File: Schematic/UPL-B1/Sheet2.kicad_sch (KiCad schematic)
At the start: 40 parts, among them K2 G5V-2_Split, P20 TestPoint, P21 TestPoint, X2 Conn_01x03_Pin_Bridge

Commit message: added majority of footprints
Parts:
- C200, C201, C202, C203, C204, C205: footprint (none) -> Capacitor_THT:C_Radial_D6.3mm_H11.0mm_P2.50mm
- C206, C207, C208, C209, C210, C211, C212, C215, C216: footprint (none) -> Capacitor_SMD:C_1206_3216Metric_Pad1.33x1.80mm_HandSolder
- D20: footprint (none) -> Package_SO:SOIC-14_3.9x8.7mm_P1.27mm
- D22: footprint SOIC127P1032X265-16N -> Package_SO:SOIC-16W_7.5x10.3mm_P1.27mm
- D23: footprint (none) -> Package_SO:SOIC-16_3.9x9.9mm_P1.27mm
- N20: footprint (none) -> Package_SO:SOIC-8_3.9x4.9mm_P1.27mm
- P20, P21: footprint (none) -> Connector_PinHeader_1.00mm:PinHeader_1x01_P1.00mm_Vertical
- R200, R201, R202, R203, R204, R205, R206, R207, R208, R209, R210, R211, R212, R215: footprint (none) -> Resistor_SMD:R_1206_3216Metric_Pad1.30x1.75mm_HandSolder
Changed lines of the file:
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@@
 			)
 		)
-		(property "Footprint" ""
+		(property "Footprint" "Package_SO:SOIC-14_3.9x8.7mm_P1.27mm"
 			(at 63.5 177.8 0)
 			(effects
@@
 			)
 		)
-		(property "Footprint" ""
+		(property "Footprint" "Resistor_SMD:R_1206_3216Metric_Pad1.30x1.75mm_HandSolder"
 			(at 328.93 227.838 90)
 			(effects
@@
 			)
 		)
-		(property "Footprint" ""
+		(property "Footprint" "Capacitor_SMD:C_1206_3216Metric_Pad1.33x1.80mm_HandSolder"
 			(at 360.68 179.07 0)
 			(effects
@@
 			)
 		)
-		(property "Footprint" ""
+		(property "Footprint" "Capacitor_SMD:C_1206_3216Metric_Pad1.33x1.80mm_HandSolder"
 			(at 116.84 35.56 0)
 			(effects
@@
 			)
 		)
-		(property "Footprint" ""
+		(property "Footprint" "Capacitor_SMD:C_1206_3216Metric_Pad1.33x1.80mm_HandSolder"
 			(at 351.79 106.68 0)
 			(effects
@@
 			)
 		)
-		(property "Footprint" ""
+		(property "Footprint" "Package_SO:SOIC-14_3.9x8.7mm_P1.27mm"
 			(at 41.91 208.28 0)
 			(effects
@@
 			)
 		)
-		(property "Footprint" ""
+		(property "Footprint" "Resistor_SMD:R_1206_3216Metric_Pad1.30x1.75mm_HandSolder"
 			(at 328.93 215.138 90)
 			(effects
@@
 			)
 		)
-		(property "Footprint" ""
+		(property "Footprint" "Capacitor_THT:C_Radial_D6.3mm_H11.0mm_P2.50mm"
 			(at 29.21 33.02 0)
 			(effects
@@
 			)
 		)
-		(property "Footprint" ""
+		(property "Footprint" "Resistor_SMD:R_1206_3216Metric_Pad1.30x1.75mm_HandSolder"
 			(at 232.918 114.3 90)
 			(effects
@@
 			)
 		)
-		(property "Footprint" ""
+		(property "Footprint" "Package_SO:SOIC-8_3.9x4.9mm_P1.27mm"
 			(at 347.98 120.65 0)
 			(effects
@@
 			)
 		)
-		(property "Footprint" ""
+		(property "Footprint" "Resistor_SMD:R_1206_3216Metric_Pad1.30x1.75mm_HandSolder"
 			(at 96.52 27.94 0)
 			(effects
@@
 			)
 		)
-		(property "Footprint" ""
+		(property "Footprint" "Resistor_SMD:R_1206_3216Metric_Pad1.30x1.75mm_HandSolder"
 			(at 236.728 165.1 90)
 			(effects
@@
 			)
 		)
-		(property "Footprint" ""
+		(property "Footprint" "Connector_PinHeader_1.00mm:PinHeader_1x01_P1.00mm_Vertical"
 			(at 121.92 22.86 0)
 			(effects
@@
 			)
 		)
-		(property "Footprint" ""
+		(property "Footprint" "Resistor_SMD:R_1206_3216Metric_Pad1.30x1.75mm_HandSolder"
 			(at 231.14 74.168 90)
 			(effects
@@
 			)
 		)
-		(property "Footprint" ""
+		(property "Footprint" "Resistor_SMD:R_1206_3216Metric_Pad1.30x1.75mm_HandSolder"
 			(at 148.59 129.54 0)
 			(effects
@@
 			)
 		)
-		(property "Footprint" ""
+		(property "Footprint" "Package_SO:SOIC-16_3.9x9.9mm_P1.27mm"
 			(at 354.33 208.28 0)
 			(effects
@@
 			)
 		)
-		(property "Footprint" ""
+		(property "Footprint" "Resistor_SMD:R_1206_3216Metric_Pad1.30x1.75mm_HandSolder"
 			(at 38.1 69.85 0)
 			(effects
@@
 			)
 		)
-		(property "Footprint" ""
+		(property "Footprint" "Capacitor_SMD:C_1206_3216Metric_Pad1.33x1.80mm_HandSolder"
 			(at 152.4 38.1 0)
 			(effects
@@
 			)
 		)
-		(property "Footprint" ""
+		(property "Footprint" "Capacitor_THT:C_Radial_D6.3mm_H11.0mm_P2.50mm"
 			(at 45.72 33.02 0)
 			(effects
@@
 			)
 		)
-		(property "Footprint" ""
+		(property "Footprint" "Resistor_SMD:R_1206_3216Metric_Pad1.30x1.75mm_HandSolder"
 			(at 85.09 69.85 0)
 			(effects
@@
 			)
 		)
-		(property "Footprint" ""
+		(property "Footprint" "Resistor_SMD:R_1206_3216Metric_Pad1.30x1.75mm_HandSolder"
 			(at 128.27 69.85 0)
 			(effects
@@
 			)
 		)
-		(property "Footprint" ""
+		(property "Footprint" "Connector_PinHeader_1.00mm:PinHeader_1x01_P1.00mm_Vertical"
 			(at 394.97 66.04 0)
 			(effects
@@
 			)
 		)
-		(property "Footprint" ""
+		(property "Footprint" "Capacitor_SMD:C_1206_3216Metric_Pad1.33x1.80mm_HandSolder"
 			(at 151.13 77.47 0)
 			(effects
@@
 			)
 		)
-		(property "Footprint" ""
+		(property "Footprint" "Package_SO:SOIC-14_3.9x8.7mm_P1.27mm"
 			(at 168.91 38.1 0)
 			(effects
@@
 			)
 		)
-		(property "Footprint" ""
+		(property "Footprint" "Package_SO:SOIC-14_3.9x8.7mm_P1.27mm"
 			(at 41.91 226.06 0)
 			(effects
@@
 			)
 		)
-		(property "Footprint" ""
+		(property "Footprint" "Capacitor_THT:C_Radial_D6.3mm_H11.0mm_P2.50mm"
 			(at 92.71 77.47 0)
 			(effects
@@
 			)
 		)
-		(property "Footprint" ""
+		(property "Footprint" "Capacitor_THT:C_Radial_D6.3mm_H11.0mm_P2.50mm"
 			(at 60.96 33.02 0)
 			(effects
@@
 			)
 		)
-		(property "Footprint" ""
+		(property "Footprint" "Resistor_SMD:R_1206_3216Metric_Pad1.30x1.75mm_HandSolder"
 			(at 41.91 175.26 0)
 			(effects
@@
 			)
 		)
-		(property "Footprint" ""
+		(property "Footprint" "Resistor_SMD:R_1206_3216Metric_Pad1.30x1.75mm_HandSolder"
 			(at 104.14 35.56 0)
 			(effects
@@
 			)
 		)
-		(property "Footprint" "SOIC127P1032X265-16N"
+		(property "Footprint" "Package_SO:SOIC-16W_7.5x10.3mm_P1.27mm"
 			(at 279.4 129.54 0)
 			(effects
@@
 			)
 		)
-		(property "Footprint" ""
+		(property "Footprint" "Capacitor_THT:C_Radial_D6.3mm_H11.0mm_P2.50mm"
 			(at 45.72 77.47 0)
 			(effects
@@
 			)
 		)
-		(property "Footprint" ""
+		(property "Footprint" "Capacitor_SMD:C_1206_3216Metric_Pad1.33x1.80mm_HandSolder"
 			(at 322.58 107.95 0)
 			(effects
@@
 			)
 		)
-		(property "Footprint" ""
+		(property "Footprint" "Capacitor_SMD:C_1206_3216Metric_Pad1.33x1.80mm_HandSolder"
 			(at 356.87 134.62 0)
 			(effects
@@
 			)
 		)
-		(property "Footprint" ""
+		(property "Footprint" "Capacitor_THT:C_Radial_D6.3mm_H11.0mm_P2.50mm"
 			(at 135.89 77.47 0)
 			(effects
@@
 			)
 		)
-		(property "Footprint" ""
+		(property "Footprint" "Capacitor_SMD:C_1206_3216Metric_Pad1.33x1.80mm_HandSolder"
 			(at 110.49 116.84 0)
 			(effects
@@
 			)
 		)
-		(property "Footprint" ""
+		(property "Footprint" "Package_SO:SOIC-14_3.9x8.7mm_P1.27mm"
 			(at 41.91 191.77 0)
 			(effects
@@
 			)
 		)
-		(property "Footprint" ""
+		(property "Footprint" "Resistor_SMD:R_1206_3216Metric_Pad1.30x1.75mm_HandSolder"
 			(at 29.21 234.95 0)
 			(effects
@@
 			)
 		)
-		(property "Footprint" ""
+		(property "Footprint" "Resistor_SMD:R_1206_3216Metric_Pad1.30x1.75mm_HandSolder"
 			(at 328.93 204.978 90)
 			(effects
@@
 			)
 		)
-		(property "Footprint" ""
+		(property "Footprint" "Capacitor_SMD:C_1206_3216Metric_Pad1.33x1.80mm_HandSolder"
 			(at 351.79 146.05 0)
 			(effects

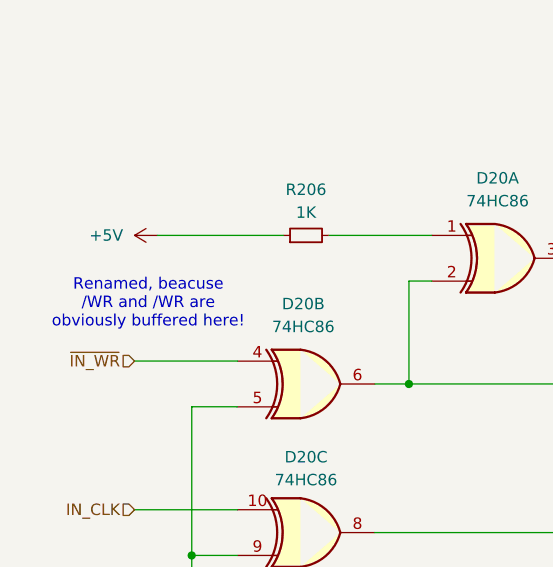
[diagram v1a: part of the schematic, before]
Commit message: Rough component outline on PCB
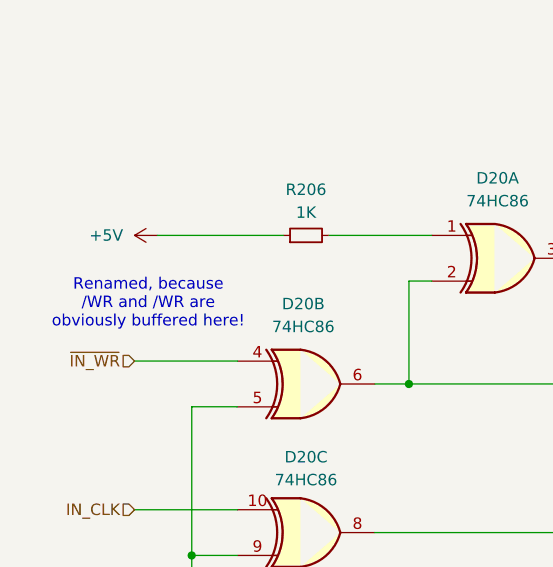
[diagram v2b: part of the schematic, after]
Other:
- note added: "Renamed, because /WR and /WR are obviously buffered here!"
- note removed: "Renamed, beacuse /WR and /WR are obviously buffered here!"
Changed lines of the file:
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@@
 		(company "BVKSound")
 	)
-	(text "Renamed, beacuse \n/WR and /WR are \nobviously buffered here!"
+	(text "Renamed, because \n/WR and /WR are \nobviously buffered here!"
 		(exclude_from_sim no)
 		(at 24.384 182.88 0)

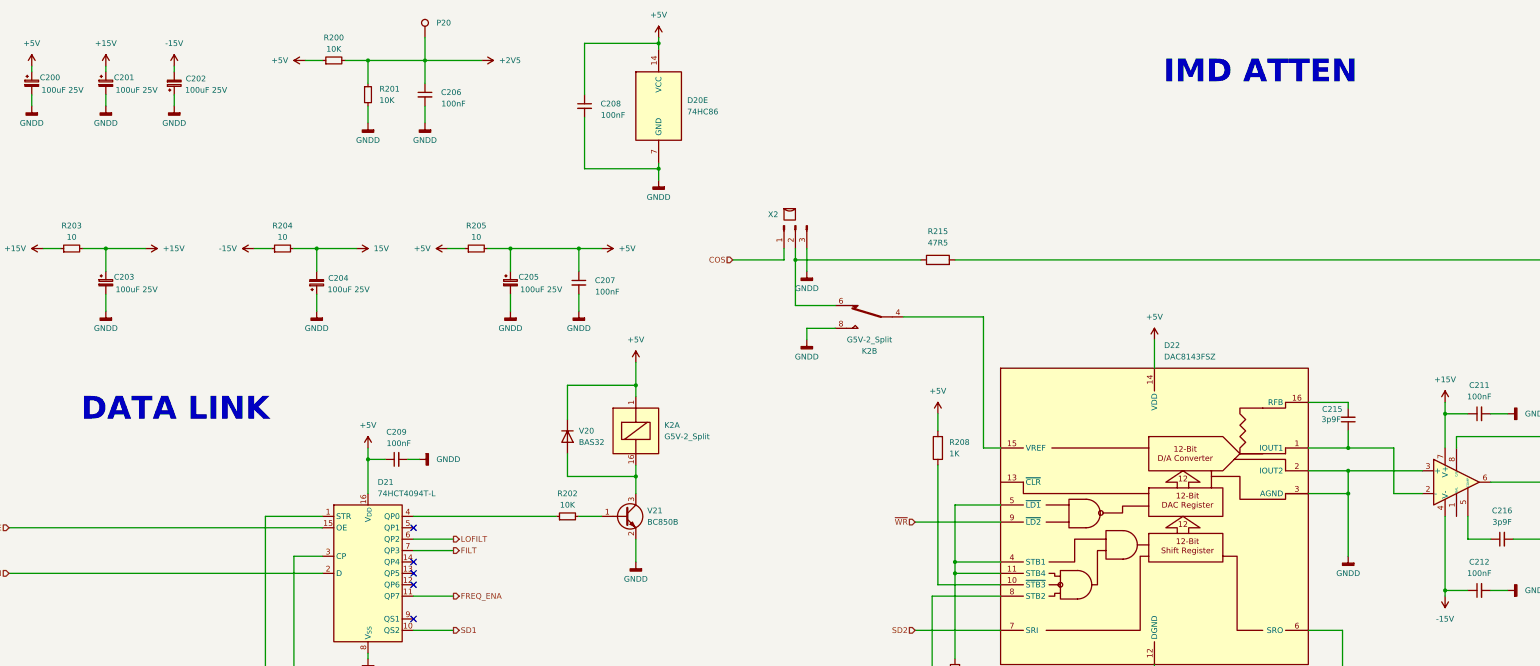
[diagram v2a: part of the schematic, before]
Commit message: ERC fixes.
- Power flags added for power nets "hanging" off resistors.
- Add missing NC-markers for intentionally unconnected parts
- Fix -15V bridge between circuits on S4/S3
- Add +5 to /CLR of DAC
- Use non-hierachical labels on main sheet.
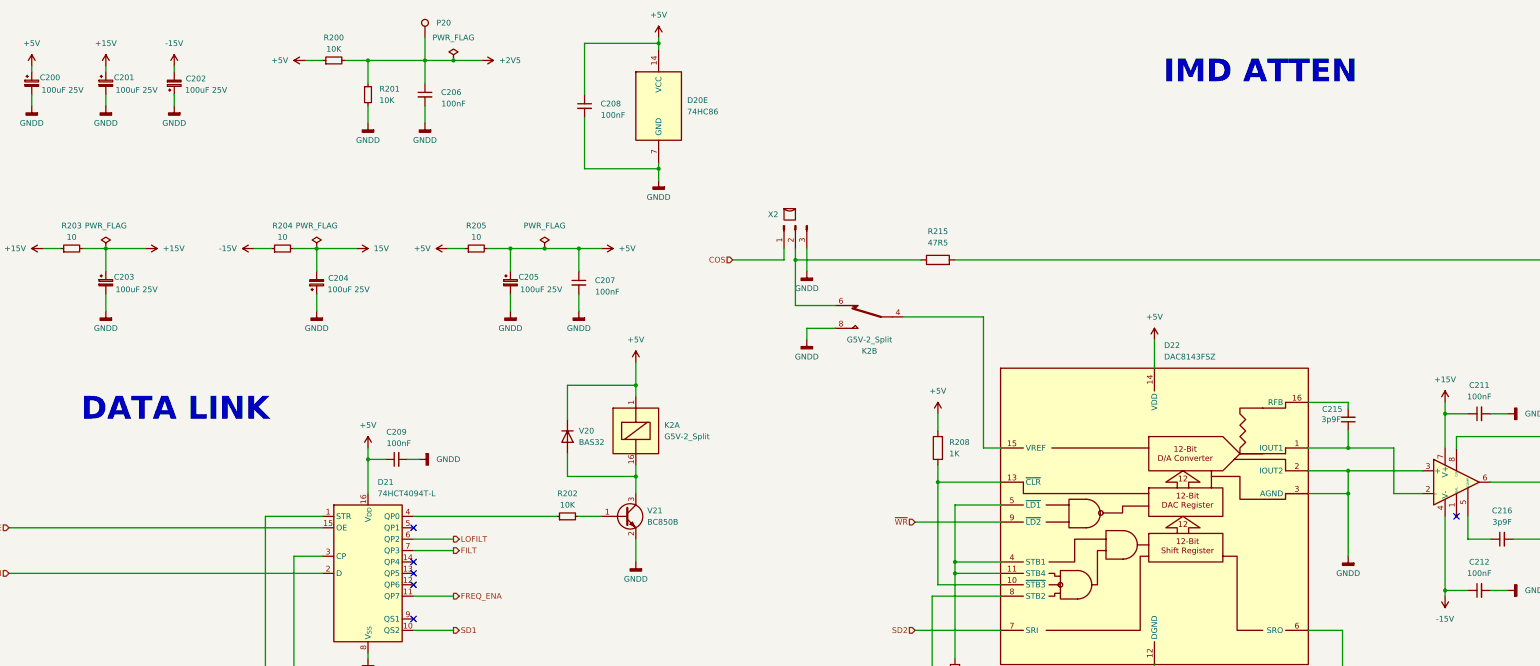
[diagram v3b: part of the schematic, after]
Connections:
- net at D22.10 (~{STB3}), R208.1: now also D22.13 (~{CLR})
- no-connect marks 6 -> 7

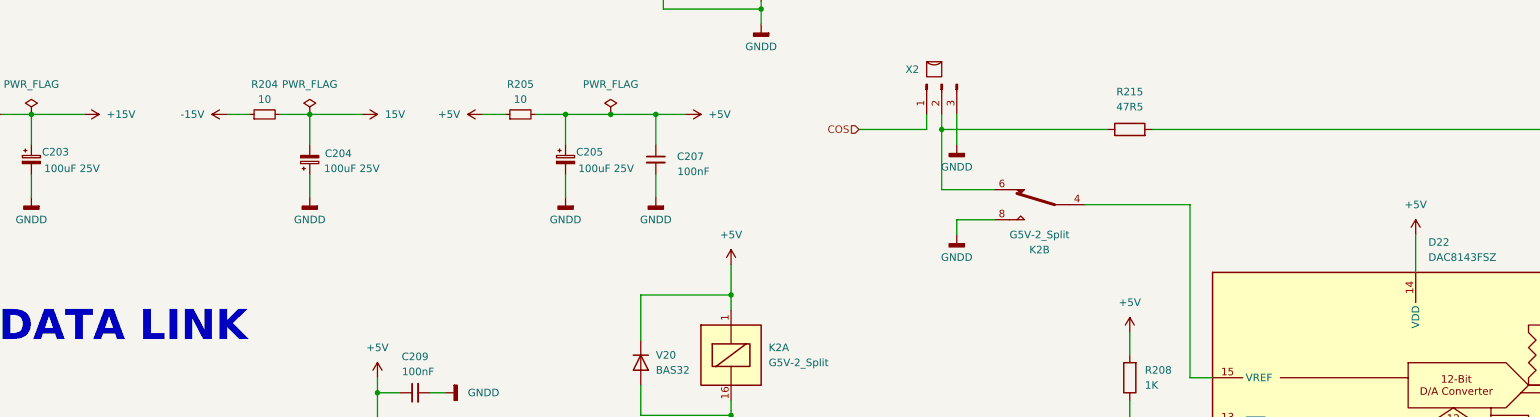
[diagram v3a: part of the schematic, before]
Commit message: Use +/-15VA for some opamps and +5VA for the DACs.
Note: Did they really use +/-15VA (denoted with asterisk in R&S
schematics) on N34 but not on N20?
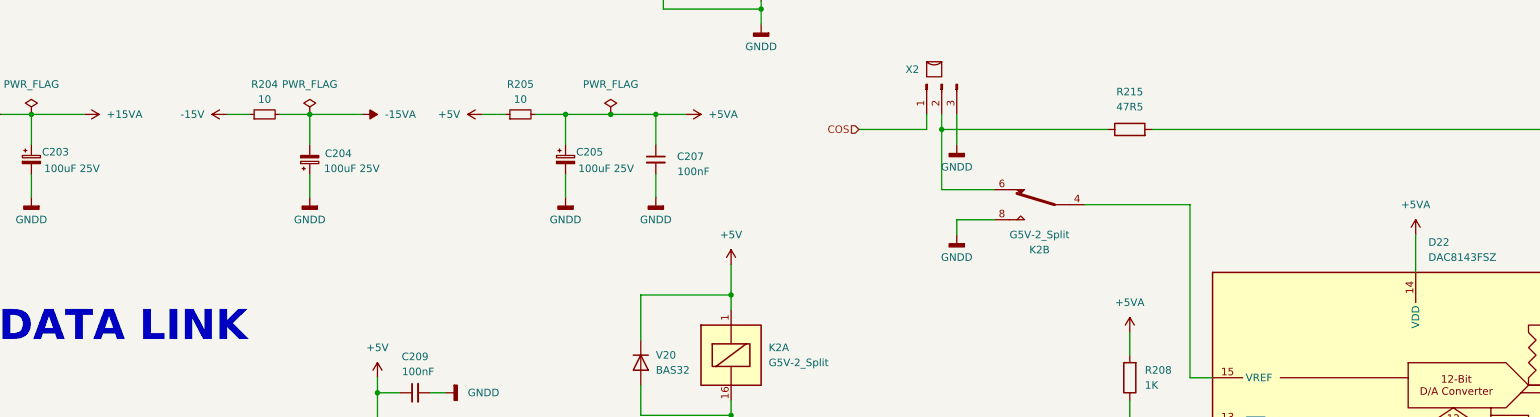
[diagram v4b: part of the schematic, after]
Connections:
- net +15V: no longer C203.1, R203.2
- net +5V: no longer C205.1, C207.1, D22.14 (VDD), R205.2, R208.2
- net 15V renamed -15VA
- new net +15VA: C203.1, R203.2
- new net +5VA: C205.1, C207.1, D22.14 (VDD), R205.2, R208.2
